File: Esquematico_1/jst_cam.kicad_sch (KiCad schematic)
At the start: 19 parts, among them J1 Screw_Terminal_01x04, J2 Screw_Terminal_01x03, J3 Screw_Terminal_01x06, J4 Screw_Terminal_01x08, J5 SWD, J6 Screw_Terminal_01x04, J7 USB_C_Receptacle_USB2.0_16P, J8 Screw_Terminal_01x01, J9 Screw_Terminal_01x01, U5 USBLC6-2SC6

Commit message: Cambios de Diodos
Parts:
- added D2: D_ST, Diode_SMD:D_SOD-323_HandSoldering, symbol Device:D_Schottky
- D3: footprint Package_TO_SOT_SMD:SOT-23 -> Diode_SMD:D_SOD-323_HandSoldering
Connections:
- net +3V3: now also D2.1 (K); no longer J5.2 (Pin_2)
- new net: D2.2 (A), J5.2 (Pin_2)
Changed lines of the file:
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@@
 	(wire
 		(pts
-			(xy 52.07 120.65) (xy 46.99 120.65)
+			(xy 45.72 45.72) (xy 49.53 45.72)
 		)
 		(stroke
@@
 	(wire
 		(pts
-			(xy 45.72 45.72) (xy 49.53 45.72)
+			(xy 63.5 40.64) (xy 68.58 40.64)
 		)
 		(stroke
@@
 	(wire
 		(pts
-			(xy 63.5 40.64) (xy 68.58 40.64)
+			(xy 130.81 133.35) (xy 130.81 130.81)
 		)
 		(stroke
@@
 	(wire
 		(pts
-			(xy 130.81 133.35) (xy 130.81 130.81)
+			(xy 127 50.8) (xy 127 54.61)
 		)
 		(stroke
@@
 	(wire
 		(pts
-			(xy 127 50.8) (xy 127 54.61)
+			(xy 39.37 120.65) (xy 39.37 118.11)
 		)
 		(stroke
@@
 	(wire
 		(pts
-			(xy 46.99 120.65) (xy 46.99 118.11)
+			(xy 50.8 120.65) (xy 52.07 120.65)
 		)
 		(stroke
@@
 	(wire
 		(pts
-			(xy 46.99 123.19) (xy 52.07 123.19)
+			(xy 45.72 123.19) (xy 52.07 123.19)
 		)
 		(stroke
@@
 	(wire
 		(pts
-			(xy 46.99 128.27) (xy 52.07 128.27)
+			(xy 45.72 128.27) (xy 52.07 128.27)
 		)
 		(stroke
@@
 	(wire
 		(pts
-			(xy 46.99 125.73) (xy 52.07 125.73)
+			(xy 45.72 125.73) (xy 52.07 125.73)
 		)
 		(stroke
@@
 	(wire
 		(pts
+			(xy 39.37 120.65) (xy 43.18 120.65)
+		)
+		(stroke
+			(width 0)
+			(type default)
+		)
+	)
+	(wire
+		(pts
 			(xy 139.7 137.16) (xy 139.7 135.89)
 		)
@@
 	(global_label "SWD_NRST"
 		(shape input)
-		(at 46.99 128.27 180)
+		(at 45.72 128.27 180)
 		(fields_autoplaced yes)
 		(effects
@@
 		)
 		(property "Intersheetrefs" "${INTERSHEET_REFS}"
-			(at 34.3287 128.27 0)
+			(at 33.0587 128.27 0)
 			(effects
 				(font
@@
 	(global_label "SWCLK"
 		(shape input)
-		(at 46.99 125.73 180)
+		(at 45.72 125.73 180)
 		(fields_autoplaced yes)
 		(effects
@@
 		)
 		(property "Intersheetrefs" "${INTERSHEET_REFS}"
-			(at 37.7758 125.73 0)
+			(at 36.5058 125.73 0)
 			(effects
 				(font
@@
 	(global_label "SWDIO"
 		(shape bidirectional)
-		(at 46.99 123.19 180)
+		(at 45.72 123.19 180)
 		(fields_autoplaced yes)
 		(effects
@@
 		)
 		(property "Intersheetrefs" "${INTERSHEET_REFS}"
-			(at 37.0273 123.19 0)
+			(at 35.7573 123.19 0)
 			(effects
 				(font
@@
 	(symbol
 		(lib_id "power:+3V3")
-		(at 46.99 118.11 0)
+		(at 39.37 118.11 0)
 		(unit 1)
 		(exclude_from_sim no)
@@
 		(fields_autoplaced yes)
 		(property "Reference" "#PWR037"
-			(at 46.99 121.92 0)
+			(at 39.37 121.92 0)
 			(effects
 				(font
@@
 		)
 		(property "Value" "+3V3"
-			(at 46.99 113.03 0)
+			(at 39.37 113.03 0)
 			(effects
 				(font
@@
 		)
 		(property "Footprint" ""
-			(at 46.99 118.11 0)
+			(at 39.37 118.11 0)
 			(effects
 				(font
@@
 		)
 		(property "Datasheet" ""
-			(at 46.99 118.11 0)
+			(at 39.37 118.11 0)
 			(effects
 				(font
@@
 		)
 		(property "Description" "Power symbol creates a global label with name \"+3V3\""
-			(at 46.99 118.11 0)
+			(at 39.37 118.11 0)
 			(effects
 				(font
@@
 			)
 		)
-		(property "Footprint" "Package_TO_SOT_SMD:SOT-23"
+		(property "Footprint" "Diode_SMD:D_SOD-323_HandSoldering"
 			(at 133.35 113.03 0)
 			(effects
@@
 					(unit 1)
 				)
+			)
+		)
+	)
+	(symbol
+		(lib_id "Device:D_Schottky")
+		(at 46.99 120.65 0)
+		(unit 1)
+		(exclude_from_sim no)
+		(in_bom yes)
+		(on_board yes)
+		(dnp no)
+		(fields_autoplaced yes)
+		(property "Reference" "D2"
+			(at 46.6725 114.3 0)
+			(effects
+				(font
+					(size 1.27 1.27)
+				)
+			)
+		)
+		(property "Value" "D_ST"
+			(at 46.6725 116.84 0)
+			(effects
+				(font
+					(size 1.27 1.27)
+				)
+			)
+		)
+		(property "Footprint" "Diode_SMD:D_SOD-323_HandSoldering"
+			(at 46.99 120.65 0)
+			(effects
+				(font
+					(size 1.27 1.27)
+				)
+				(hide yes)
+			)
+		)
+		(property "Datasheet" "~"
+			(at 46.99 120.65 0)
+			(effects
+				(font
+					(size 1.27 1.27)
+				)
+				(hide yes)
+			)
+		)
+		(property "Description" "Schottky diode"
+			(at 46.99 120.65 0)
+			(effects
+				(font
+					(size 1.27 1.27)
+				)
+				(hide yes)
+			)
+		)
+		(pin "1"
+		)
+		(pin "2"
+		)
+		(instances
+			(project "Esquematico_1"
+				(path "/de2d80c1-c21c-478d-b724-17659b714c38/457e76de-adfe-4ec5-a818-c5970caa89a7"
+					(reference "D2")
+					(unit 1)
+				)

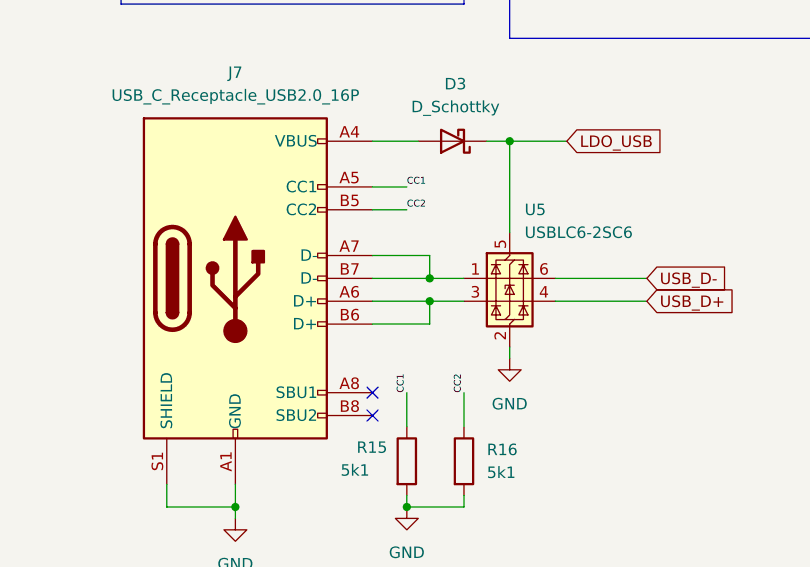
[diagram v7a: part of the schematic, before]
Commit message: Cambio de magnometro :c
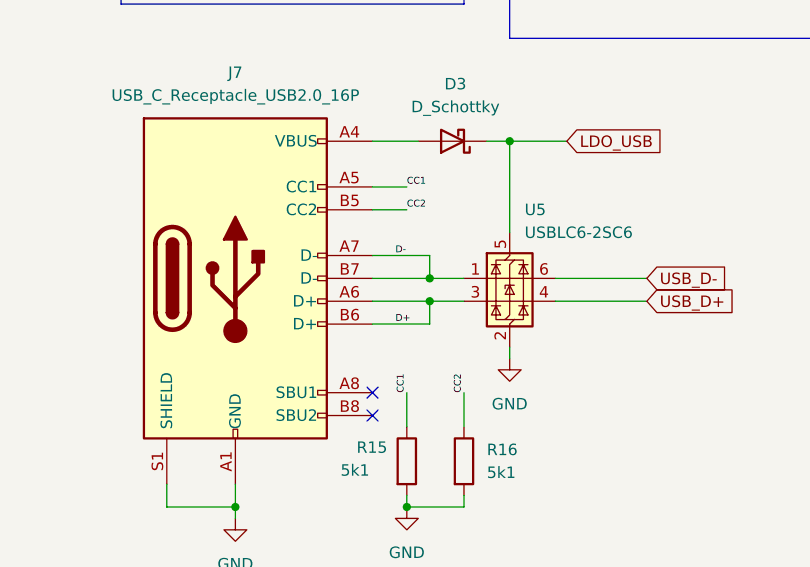
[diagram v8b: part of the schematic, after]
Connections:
- net D-: now reaches J7.A7 (D-), J7.B7 (D-), U5.1 (I/O1)
- net D+: now reaches J7.A6 (D+), J7.B6 (D+), U5.3 (I/O2)
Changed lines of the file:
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@@
+		)
+	)
+	(label "D+"
+		(at 127 133.35 0)
+		(effects
+			(font
+				(size 0.762 0.762)
+			)
+			(justify left bottom)
 		)
 	)
@@
 		(effects
 			(font
+				(size 0.762 0.762)
+			)
+			(justify left bottom)
+		)
+	)
+	(label "D-"
+		(at 127 125.73 0)
+		(effects
+			(font
